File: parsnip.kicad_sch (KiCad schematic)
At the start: 70 parts, among them J1 SPI BUS, J2 I2C3, J3 I2C1, J4 I2C2, J5 e-Ink Display Connector, J6 UART0, SW1 ESP_RESET, SW2 BOOT, U1 ESP32-S3-WROOM-1-N16R8, Y1 32.768kHz

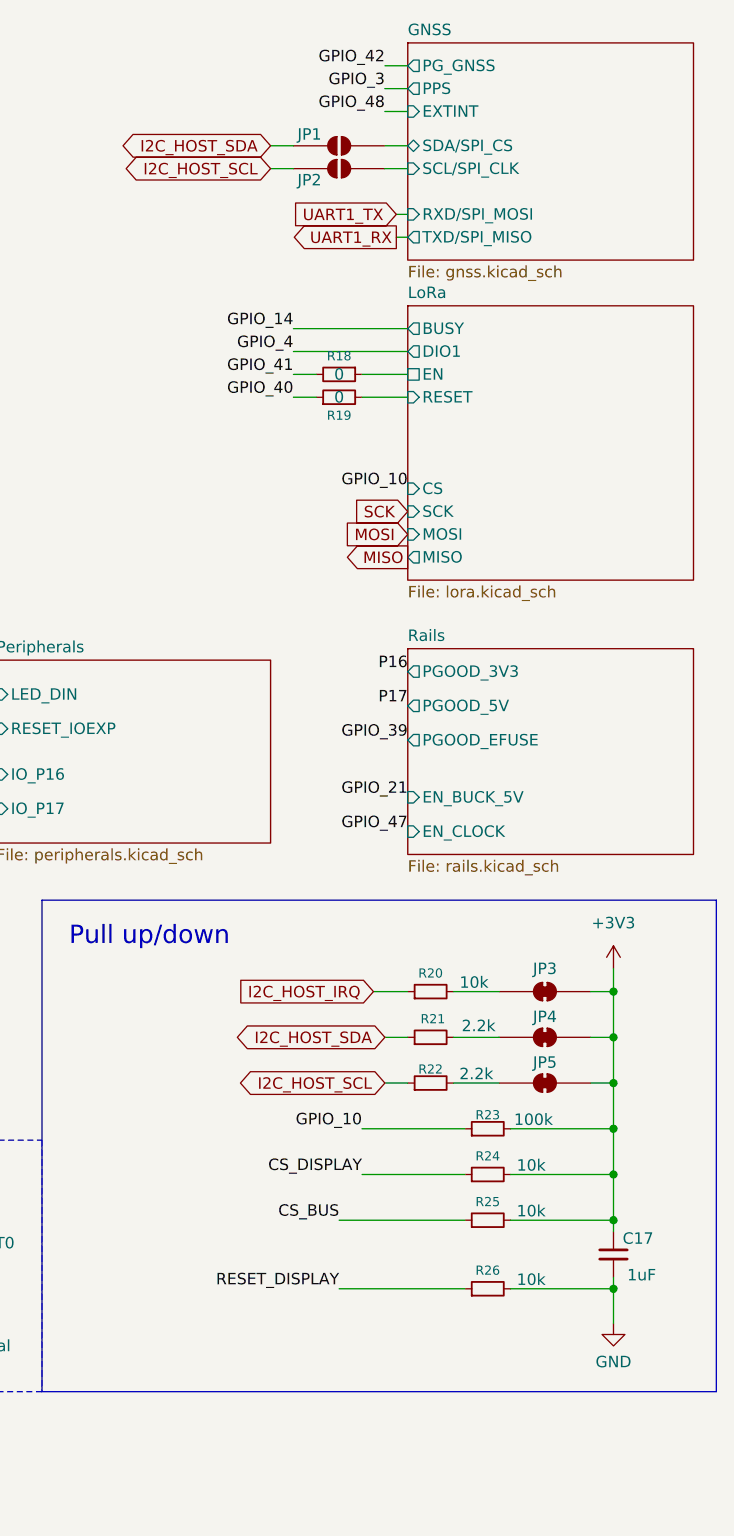
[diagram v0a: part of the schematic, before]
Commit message: schematic: add D24/D25 PZU12B2L zeners, Q_NMOS_SGD symbol, misc sheet edits
Co-Authored-By: Claude Opus 5.5 <noreply@anthropic.com>
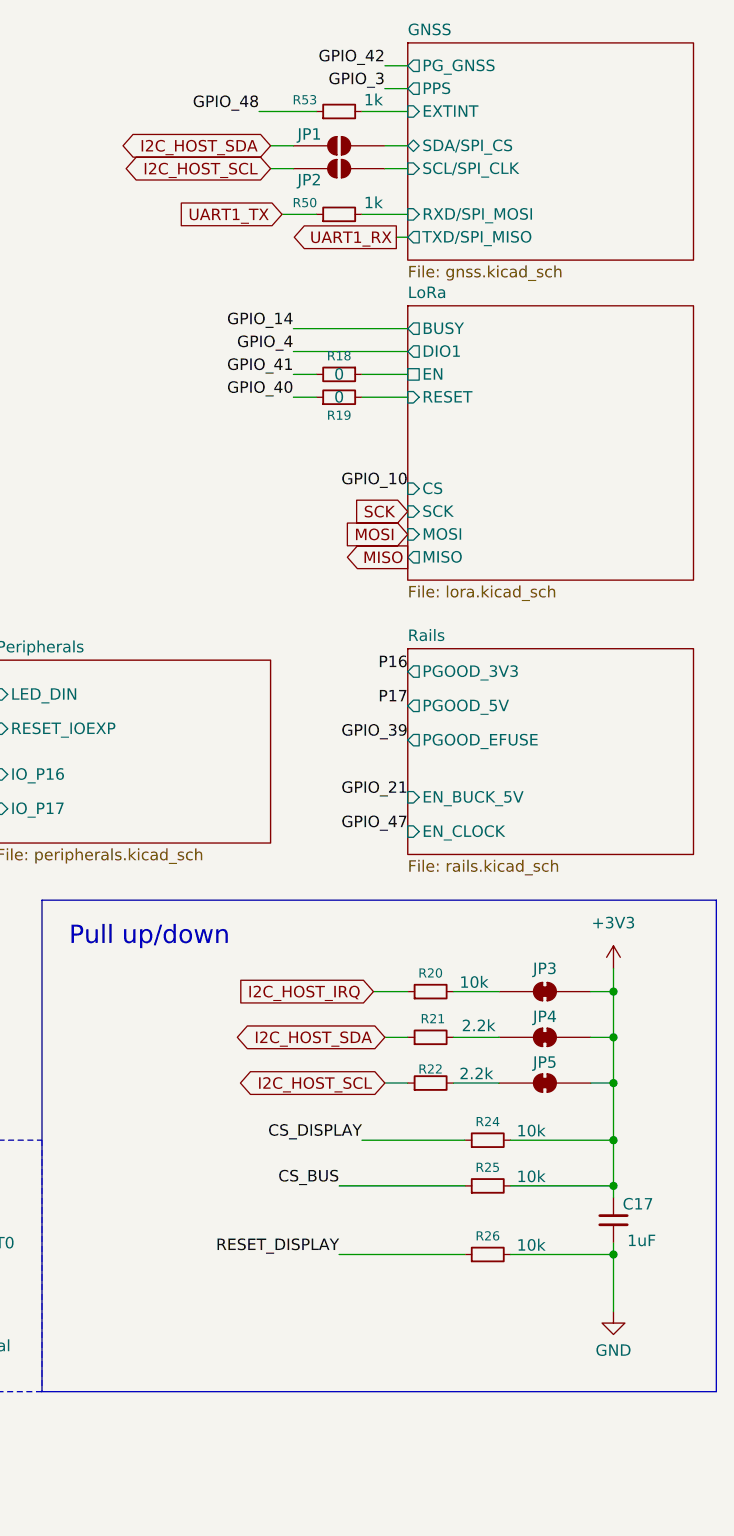
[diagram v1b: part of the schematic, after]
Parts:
- removed R23: 100k, Resistor_SMD:R_0402_1005Metric_Pad0.72x0.64mm_HandSolder, symbol Device:R_Small
- added R50, R53: 1k, Resistor_SMD:R_0402_1005Metric, symbol Device:R_Small
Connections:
- net GPIO_48: now also R53.1
- net UART1_TX: now also R50.1
- new net GNSS/EXTINT: R53.2
- new net GNSS/RXD/SPI_MOSI: R50.2
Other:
- moved on the sheet: C17, R24, R25, R26

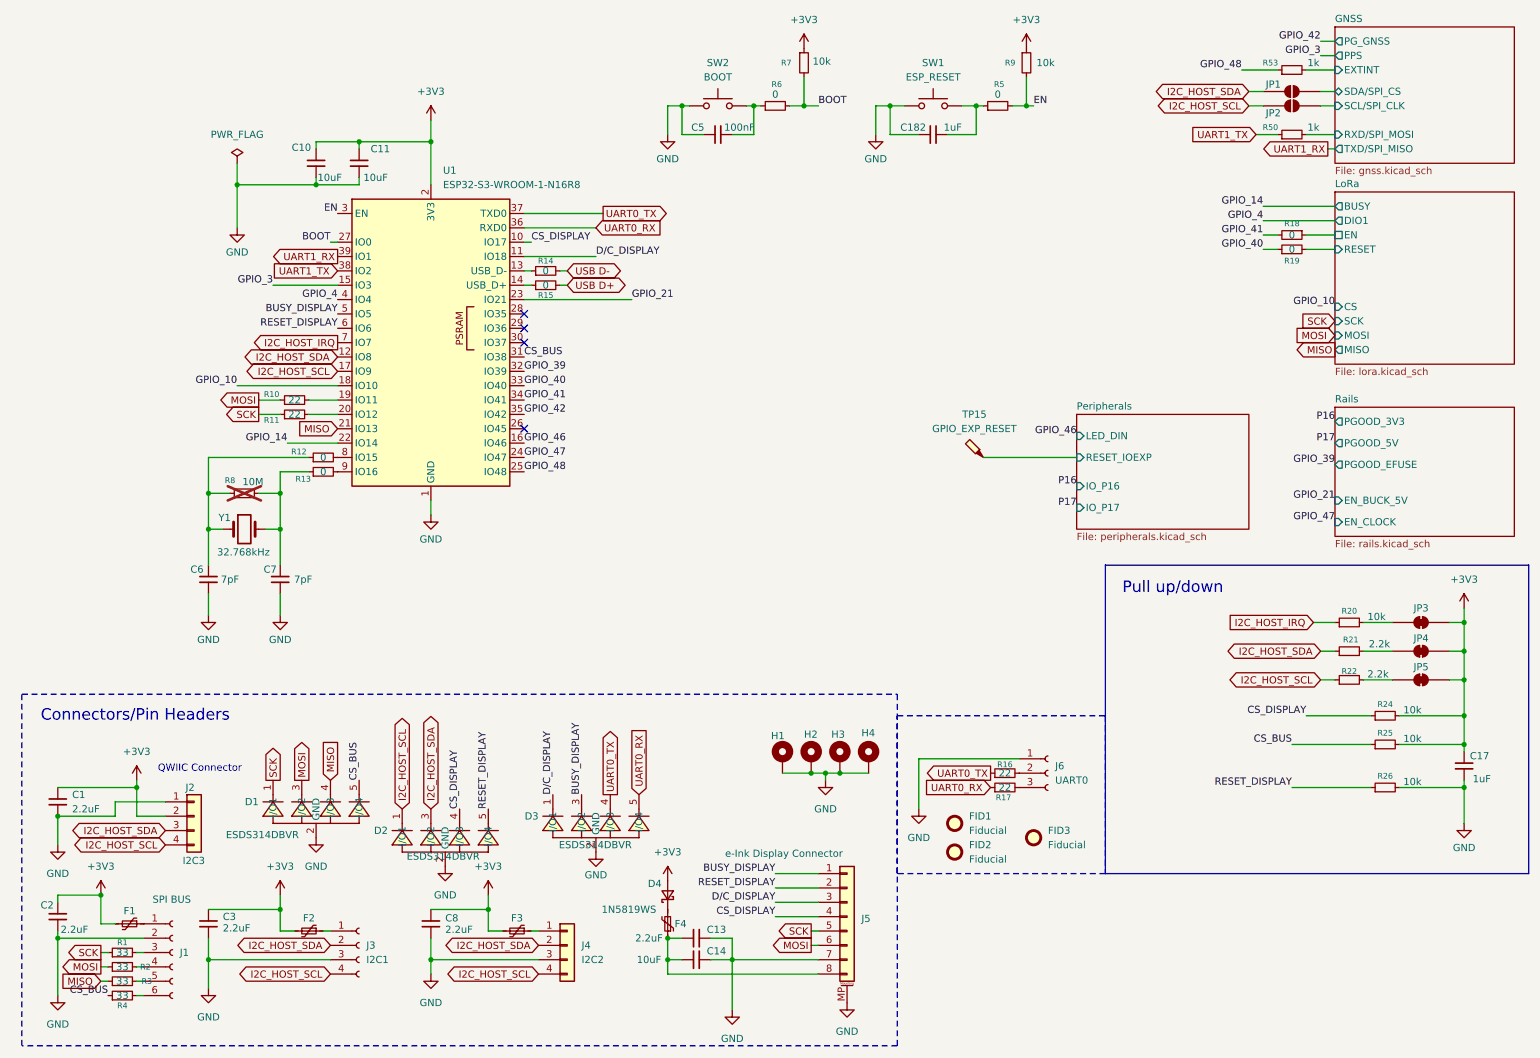
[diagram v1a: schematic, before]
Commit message: checkpoint: schematic WIP before battery -> charger rename
Connectors and Overview sheets, LSM6DSV16X/TPS22945/charger datasheets,
and in-progress edits across all sheets, committed as-is so the rename
diff stands alone.

Co-Authored-By: Claude Opus 5.5 <noreply@anthropic.com>
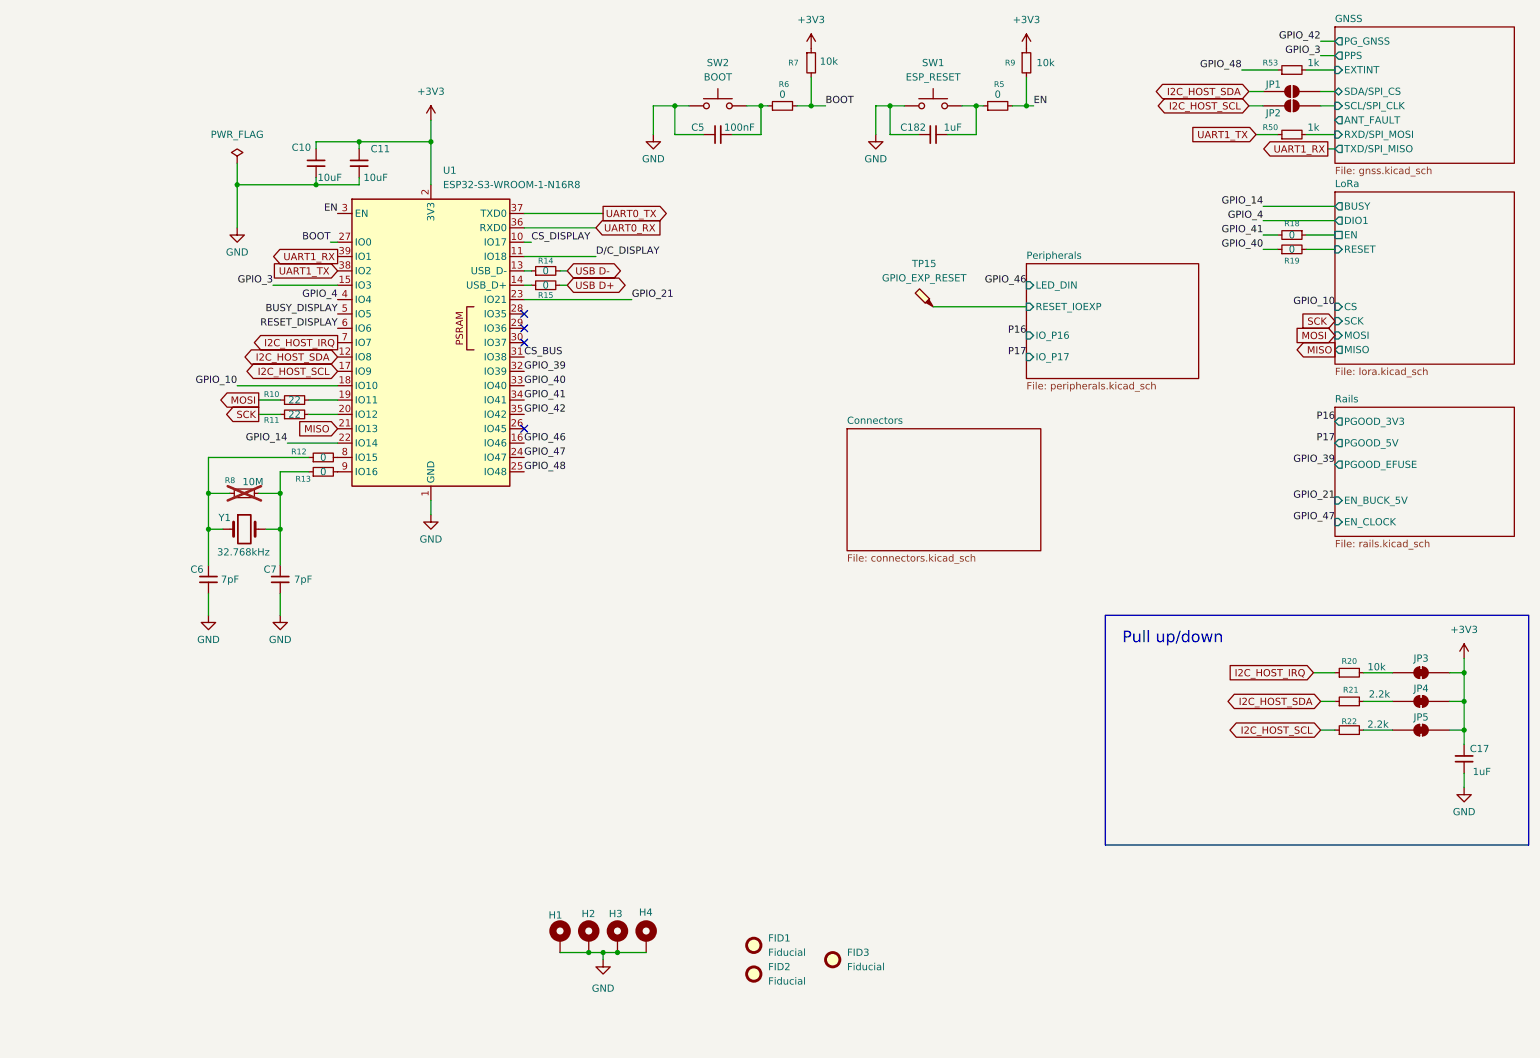
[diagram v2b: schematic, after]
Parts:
- removed C1, C13, C2, C3, C8: 2.2uF, Capacitor_SMD:C_0402_1005Metric, symbol Device:C_Small
- removed C14: 10uF, Capacitor_SMD:C_0805_2012Metric, symbol Device:C_Small
- removed D1, D2, D3: ESDS314DBVR, Package_TO_SOT_SMD:SOT-23-5, symbol easyeda2kicad:ESDS314DBVR-TP
- removed D4: 1N5819WS, Diode_SMD:D_SOD-323, symbol Device:D_Schottky_Small
- removed F1, F3: 1A hold, Fuse:Fuse_0805_2012Metric, symbol Device:Polyfuse_Small
- removed F2: 2A hold, Fuse:Fuse_0805_2012Metric, symbol Device:Polyfuse_Small
- removed F4: 350mA hold, Fuse:Fuse_0805_2012Metric, symbol Device:Polyfuse_Small
- removed J1: SPI BUS, easyeda2kicad:HDR-SMD_6P-P2.54-H-F-W11.7, symbol Connector:Conn_01x06_Socket
- removed J2: I2C3, Connector_JST:JST_SH_SM04B-SRSS-TB_1x04-1MP_P1.00mm_Horizontal, symbol Connector_Generic:Conn_01x04
- removed J3: I2C1, easyeda2kicad:CONN-SMD_4P-P2.54_HX-PM2.54-1X4PWT, symbol Connector:Conn_01x04_Socket
- removed J4: I2C2, Connector_PinSocket_2.54mm:PinSocket_1x04_P2.54mm_Vertical, symbol Connector_Generic:Conn_01x04
- removed J5: e-Ink Display Connector, Connector_Molex:Molex_PicoBlade_53261-0871_1x08-1MP_P1.25mm_Horizontal, symbol Connector_Generic_MountingPin:Conn_01x08_MountingPin
- removed J6: UART0, Connector_JST:JST_SH_SM03B-SRSS-TB_1x03-1MP_P1.00mm_Horizontal, symbol Connector:Conn_01x03_Socket
- removed R1, R2, R3, R4: 33, Resistor_SMD:R_0402_1005Metric_Pad0.72x0.64mm_HandSolder, symbol Device:R_Small
- removed R16, R17: 22, Resistor_SMD:R_0402_1005Metric, symbol Device:R_Small
- removed R24, R25, R26: 10k, Resistor_SMD:R_0402_1005Metric_Pad0.72x0.64mm_HandSolder, symbol Device:R_Small
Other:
- added sheet Connectors (connectors.kicad_sch)
- sheet GNSS ports: added ANT_FAULT; removed none
- note removed: "Connectors/Pin Headers"
- note removed: "QWIIC Connector"
- title: MCU + GPIO -> ESP32-S3 MCU
- moved on the sheet: C17, JP3, JP4, JP5, R20, R21, R22, R6, R7, TP15
